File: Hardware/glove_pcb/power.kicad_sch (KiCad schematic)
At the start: 7 parts, among them U1 AP63205WU

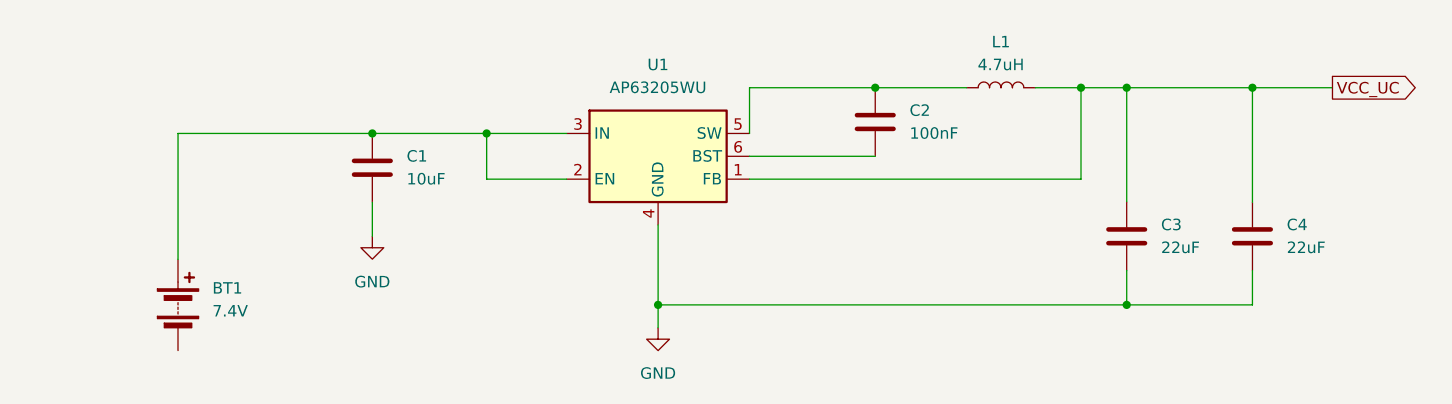
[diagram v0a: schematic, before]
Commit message: Replace offboard components with connectors, add uC, add example mux, fix motor wiring
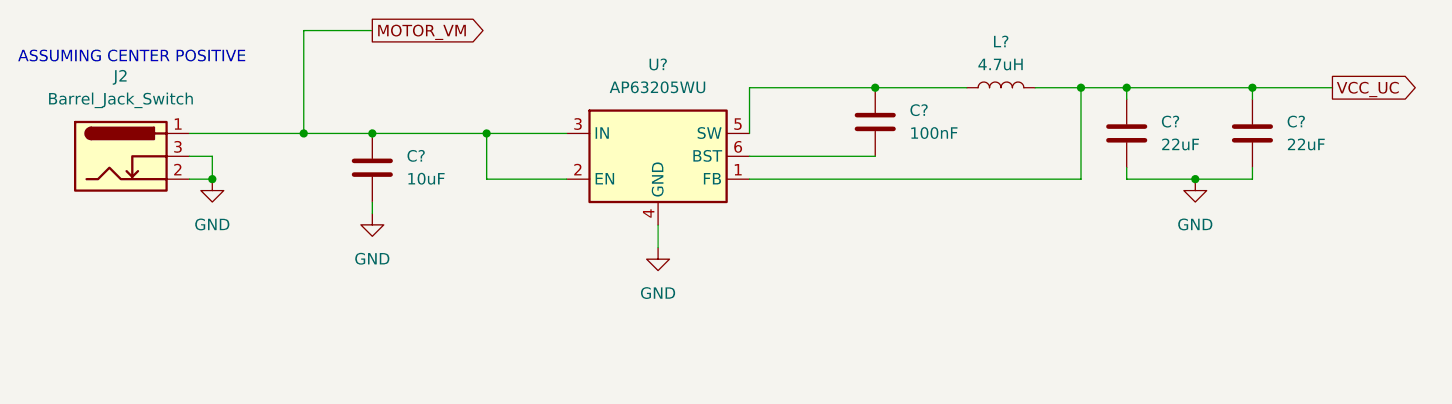
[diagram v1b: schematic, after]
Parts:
- removed BT1: 7.4V, symbol Device:Battery
- added J2: Barrel_Jack_Switch, symbol Connector:Barrel_Jack_Switch
- renumbered C3 to C?, C2 to C?, C4 to C?, C1 to C?, L1 to L?, U1 to U?
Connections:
- net GND: now also J2.2, J2.3
- net MOTOR_VM: now reaches C?.1, U?.2 (EN), U?.3 (IN)
- net MOTOR_VM: now also J2.1
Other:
- note added: "ASSUMING CENTER POSITIVE"
- moved on the sheet: C?

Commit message: Finish controller pin assignments
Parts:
- added C?: 100nF, symbol Device:C
- added C? (x2): 22uF, symbol Device:C
- added C?: 10uF, symbol Device:C
- added L?: 4.7uH, symbol Device:L
- added U5: AP63203WU, Package_TO_SOT_SMD:TSOT-23-6, symbol Regulator_Switching:AP63203WU
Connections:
- net GND: now also C?.2, C?.2, C?.2, U5.4 (GND)
- net VCC_UC: now also C?.1, U5.2 (EN), U5.3 (IN)
- new net: C?.1, L?.1, U5.5 (SW)
- new net: C?.2, U5.6 (BST)
- new net VCC_BT: C?.1, C?.1, L?.2, U5.1 (FB)
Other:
- note added: "3.3V -> HC-05"
- note added: "5V -> ATmega"

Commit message: Yet more improvements to the schematic
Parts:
- removed C?: 100nF, symbol Device:C
- removed C? (x2): 22uF, symbol Device:C
- removed C?: 10uF, symbol Device:C
- removed L?: 4.7uH, symbol Device:L
- removed U5: AP63203WU, Package_TO_SOT_SMD:TSOT-23-6, symbol Regulator_Switching:AP63203WU
- added C8: 1mF, symbol Device:C_Polarized
- added C? (x2): 0.1uF, symbol Device:C
- added D1, D2: D, symbol Device:D
- added U5: TCR2EF33_LMCT, SOT-25 SMV_TOS, symbol Glove_Symbols:TCR2EF33_LMCT
- C?: value 100nF -> 0.1uF
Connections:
- net GND: now also C8.2, C?.2, C?.2, U5.2 (GND)
- net MOTOR_VM: now also C8.1, D1.1 (K)
- net VCC_BT: now also C?.1, D2.2 (A), U5.5 (VOUT)
- net VCC_UC: now also C?.1, D2.1 (K), U5.1 (VIN), U5.3 (CONTROL)
- net at C?.1, L?.1, U?.5 (SW): now also D1.2 (A)
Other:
- moved on the sheet: J2

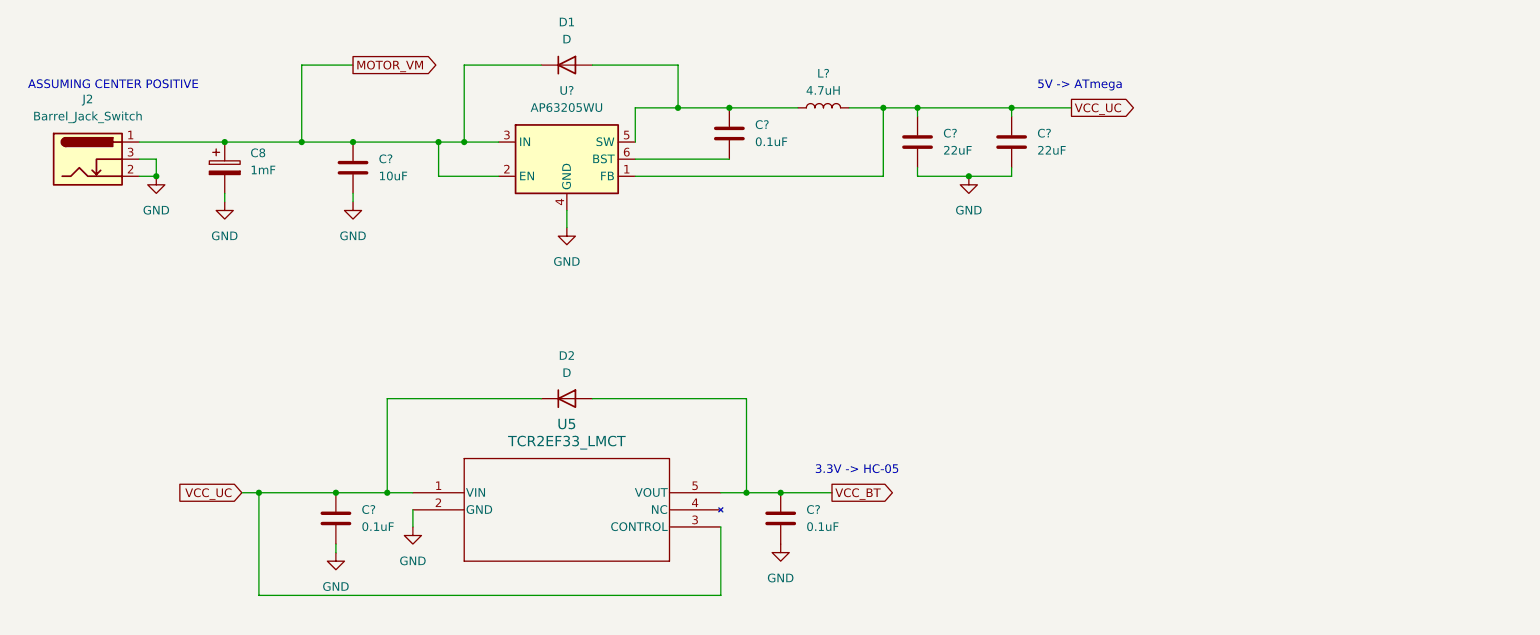
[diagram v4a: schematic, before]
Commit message: Finish schematic
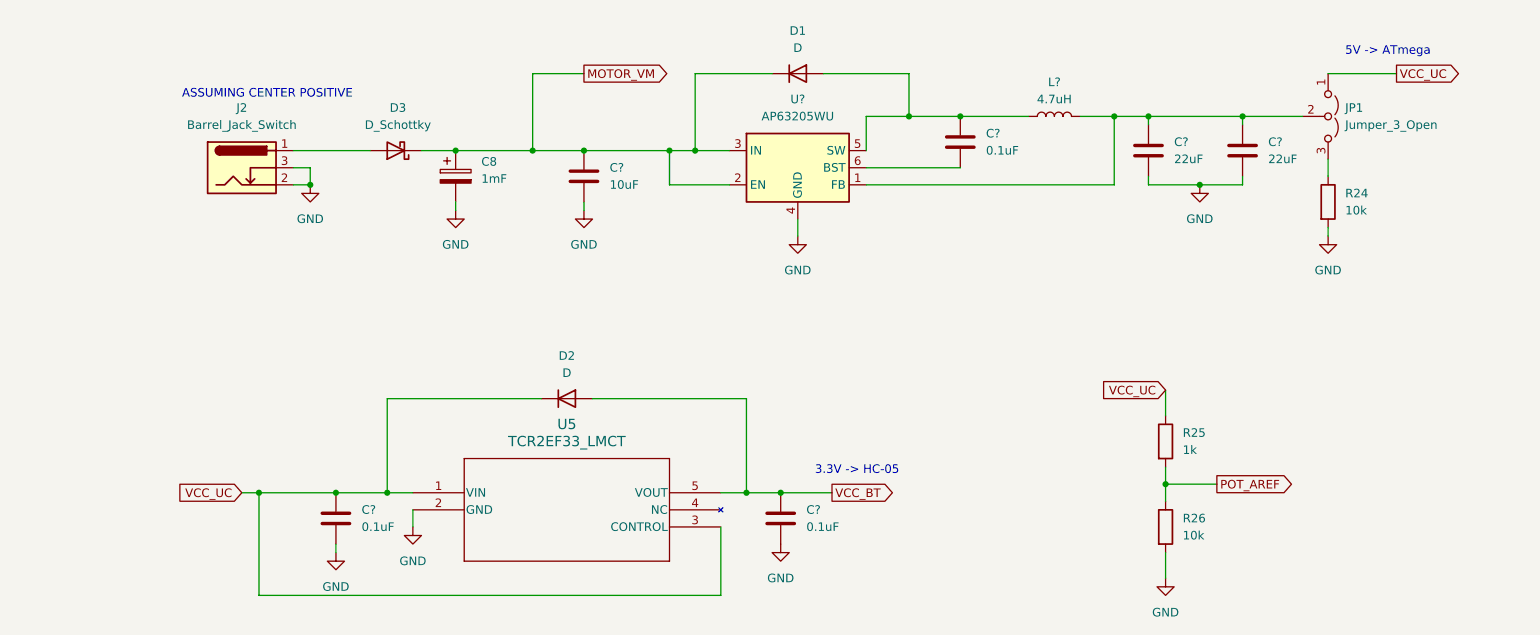
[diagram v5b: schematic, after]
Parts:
- added D3: D_Schottky, symbol Device:D_Schottky
- added JP1: Jumper_3_Open, symbol Jumper:Jumper_3_Open
- added R24, R26: 10k, symbol Device:R
- added R25: 1k, symbol Device:R
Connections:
- net GND: now also R24.2, R26.2
- net MOTOR_VM: now also D3.1 (K); no longer J2.1
- net VCC_UC: now also JP1.1 (A), R25.1; no longer C?.1, C?.1, L?.2, U?.1 (FB)
- new net: JP1.3 (B), R24.1
- new net: C?.1, C?.1, JP1.2 (C), L?.2, U?.1 (FB)
- new net: D3.2 (A), J2.1
- new net POT_AREF: R25.2, R26.1
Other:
- moved on the sheet: C8, C?, D1, J2, L?, U?

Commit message: Add titles to pages and reannotate
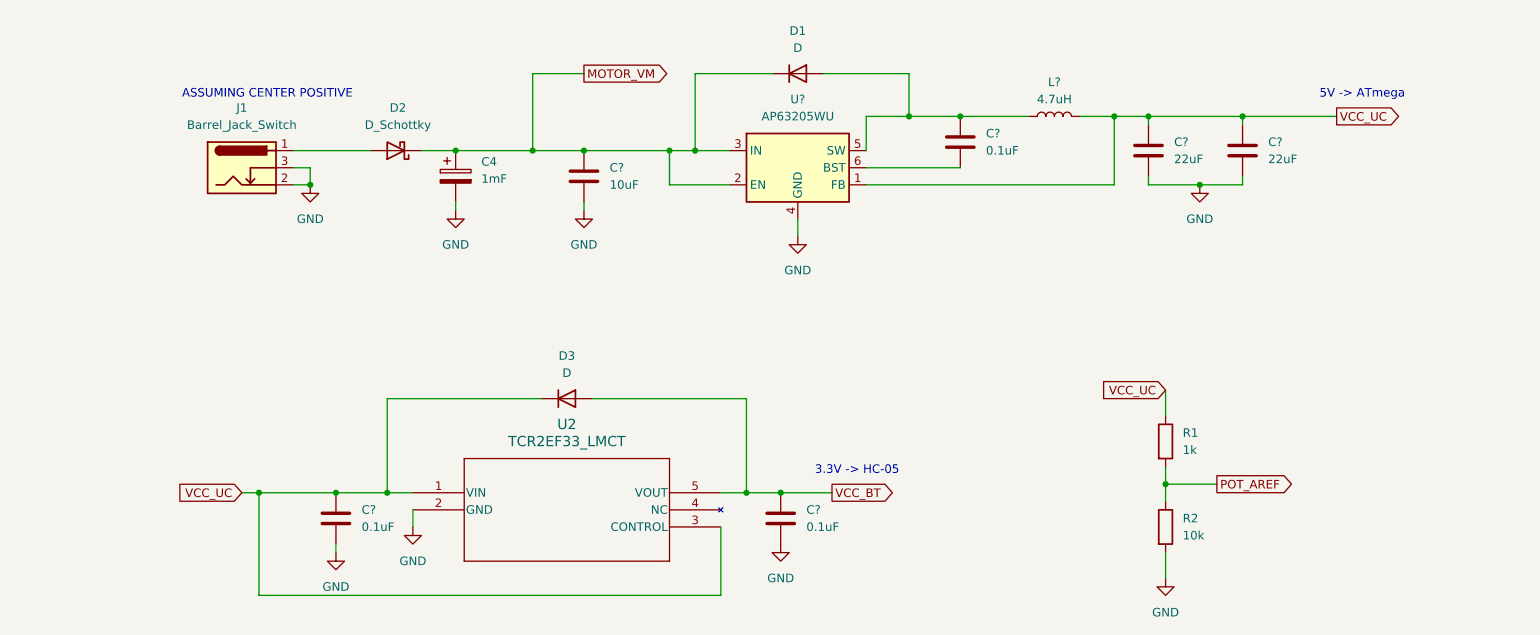
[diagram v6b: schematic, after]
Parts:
- removed JP1: Jumper_3_Open, symbol Jumper:Jumper_3_Open
- removed R24: 10k, symbol Device:R
- renumbered C8 to C4, D3 to D2, D2 to D3, J2 to J1, R25 to R1, R26 to R2, U5 to U2
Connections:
- net VCC_UC: now also C?.1, C?.1, L?.2, U?.1 (FB)
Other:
- company: (none) -> COEN 490 Team 15
- title: (none) -> Power Supply
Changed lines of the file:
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@@
 (kicad_sch (version 20230121) (generator eeschema)
   (paper "USLetter")
+  (title_block
+    (title "Power Supply")
+    (date "2023-11-24")
+    (company "COEN 490 Team 15")
+  )

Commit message: Finalize schematic for real this time
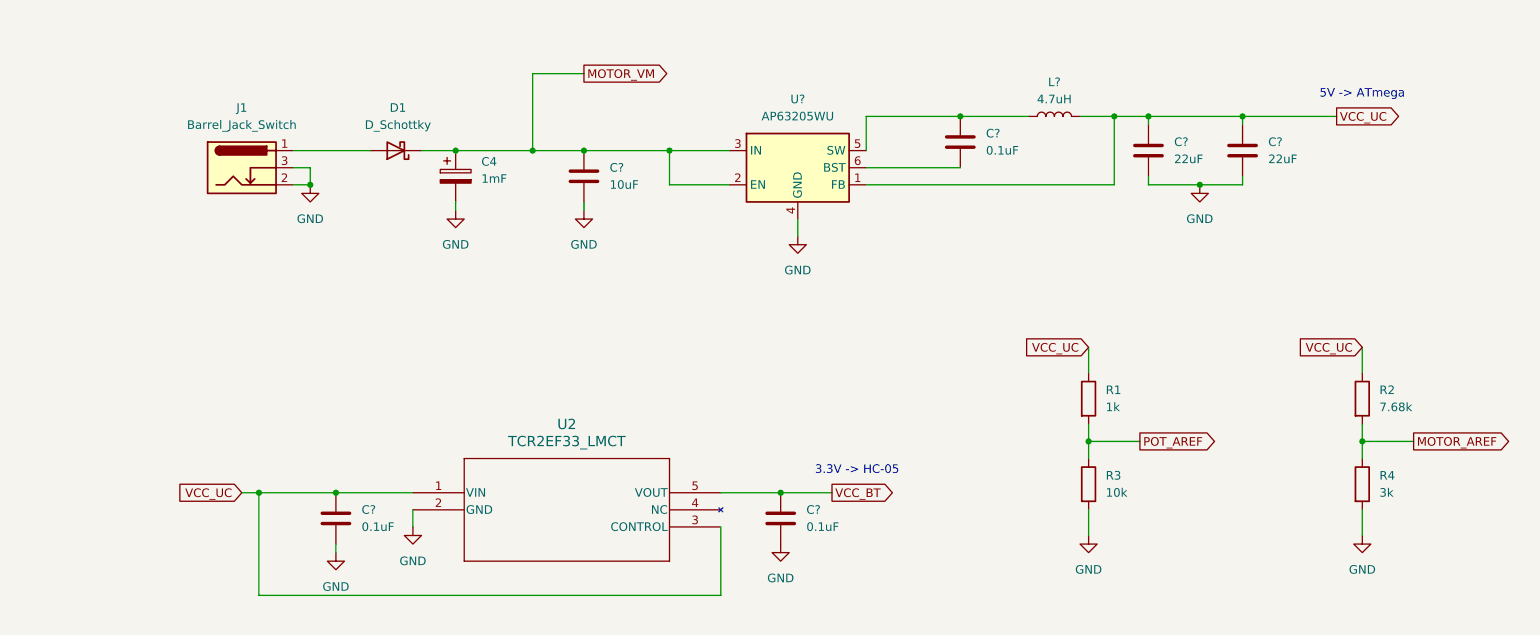
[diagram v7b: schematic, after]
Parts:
- removed D1, D3: D, symbol Device:D
- added R2: 7.68k, symbol Device:R
- added R4: 3k, symbol Device:R
- renumbered D2 to D1, R2 to R3
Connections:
- net GND: now also R4.2
- net VCC_UC: now also R2.1
- new net MOTOR_AREF: R2.2, R4.1
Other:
- note removed: "ASSUMING CENTER POSITIVE"
- moved on the sheet: R1, R3

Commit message: Added Footprints
I Added footprints for every components in PCB
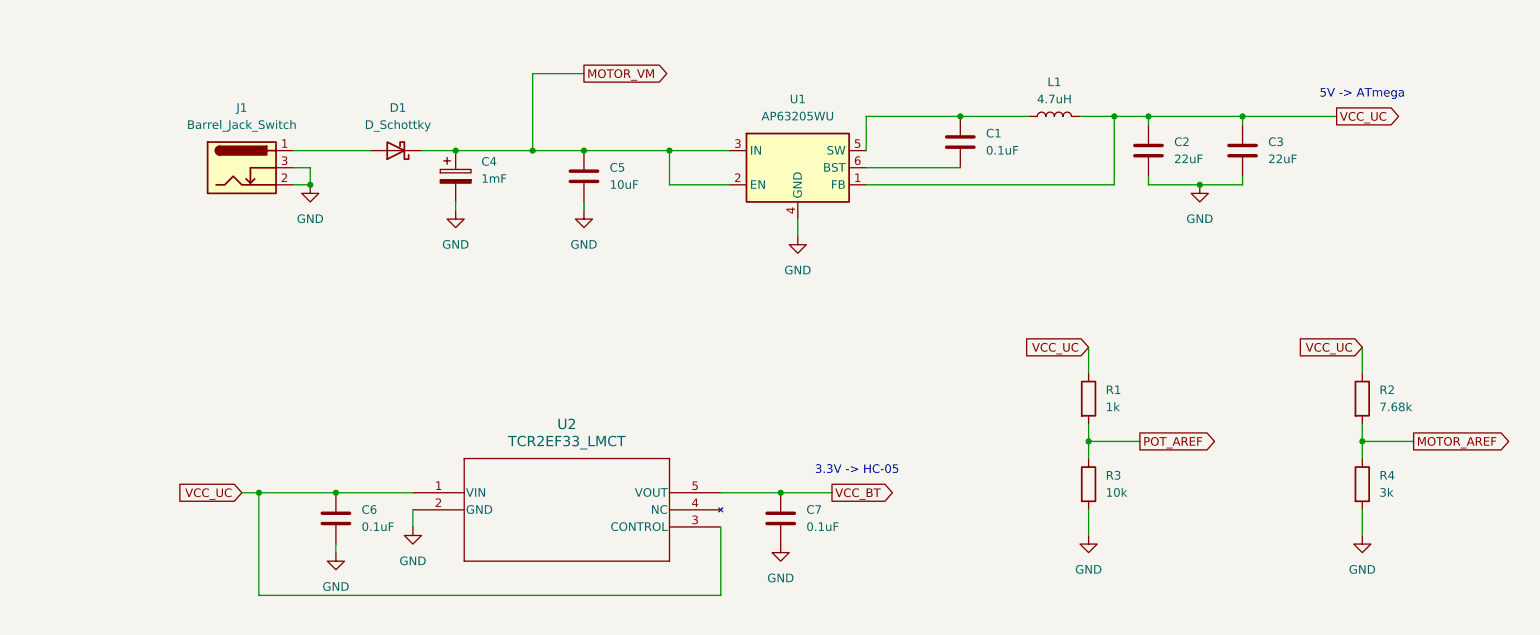
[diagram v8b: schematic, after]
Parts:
- C1, C6, C7: renamed from C?; footprint (none) -> Capacitor_SMD:C_0603_1608Metric_Pad1.08x0.95mm_HandSolder
- C2, C3: renamed from C?; footprint (none) -> Capacitor_SMD:C_0805_2012Metric_Pad1.18x1.45mm_HandSolder
- C4: footprint (none) -> Capacitor_THT:CP_Radial_D10.0mm_P5.00mm
- C5: renamed from C?; footprint (none) -> Capacitor_SMD:C_1206_3216Metric_Pad1.33x1.80mm_HandSolder
- D1: footprint (none) -> Package_TO_SOT_SMD:TO-263-3_TabPin2
- J1: footprint (none) -> Connector_BarrelJack:BarrelJack_Wuerth_694108106102_2.5x5.5mm
- L1: renamed from L?; footprint (none) -> Inductor_SMD:L_0805_2012Metric_Pad1.05x1.20mm_HandSolder
- R1, R3, R4: footprint (none) -> Resistor_SMD:R_0805_2012Metric_Pad1.20x1.40mm_HandSolder
- R2: footprint (none) -> Resistor_SMD:R_1206_3216Metric_Pad1.30x1.75mm_HandSolder
- gave numbers to parts that had none: 1
